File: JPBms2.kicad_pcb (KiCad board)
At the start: 2 copper layers, 65 x 35 mm, 23 parts, among them J1 Conn_ARM_SWD_TagConnect_TC2030, J2 Barrel_Jack_MountingPin, U1 ST715M25R, U2 STM32L053R8Tx, U3 ZXCT1107

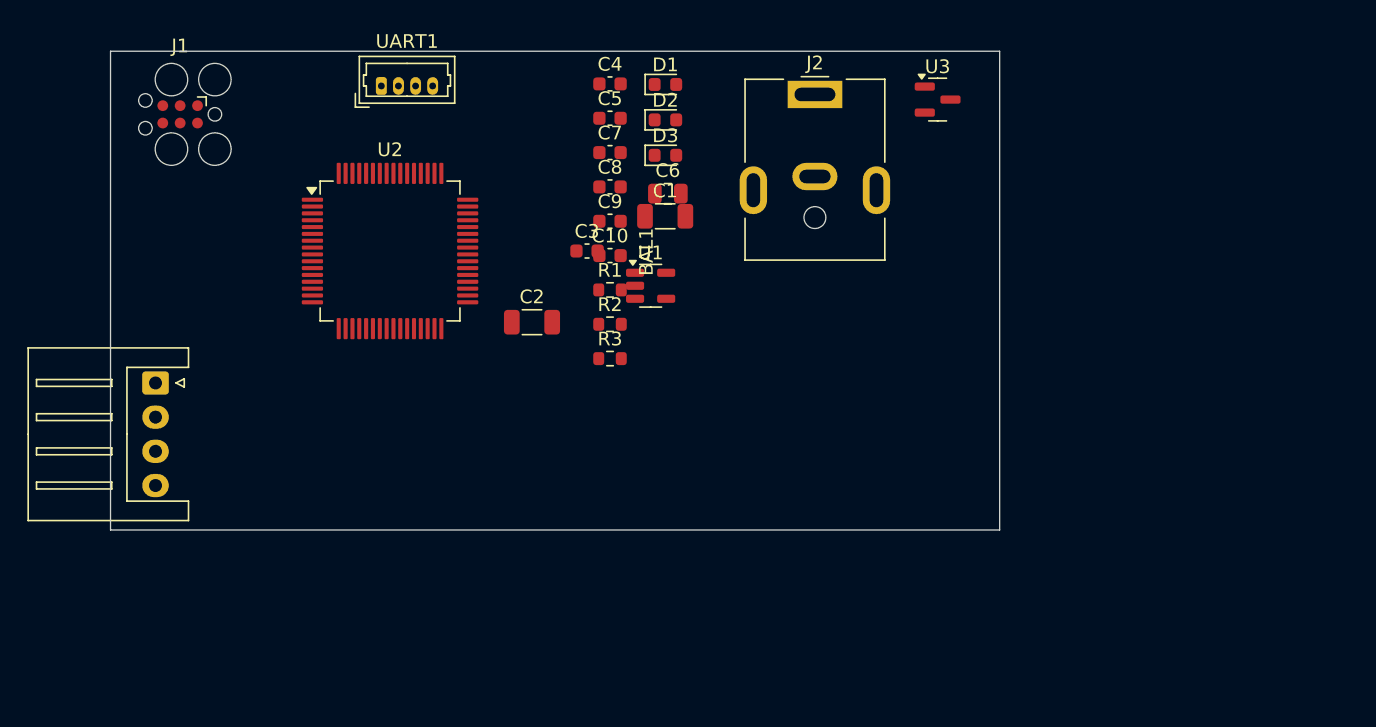
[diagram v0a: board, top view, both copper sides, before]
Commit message: Some part selections
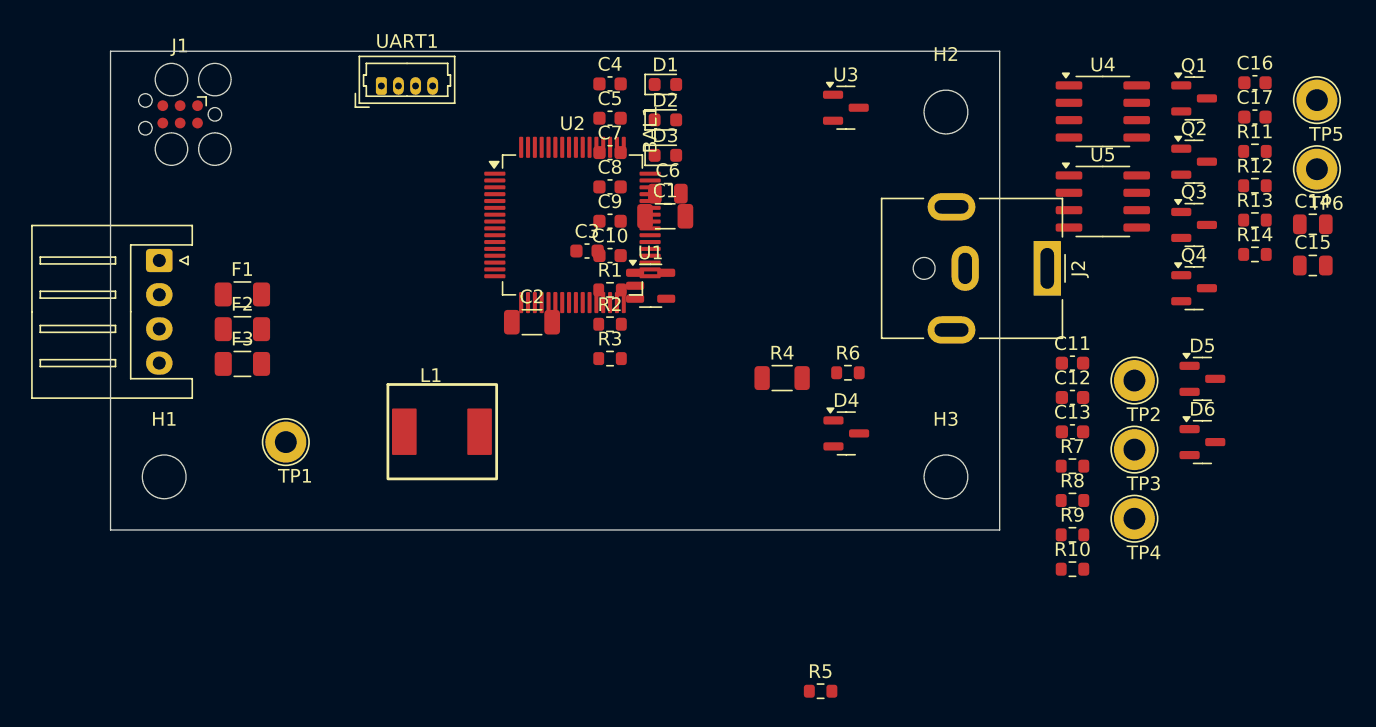
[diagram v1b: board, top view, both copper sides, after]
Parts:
- added C11: 10p, Capacitor_SMD:C_0603_1608Metric, F.Cu at (147.0, 104.1)
- added C12: 1n, Capacitor_SMD:C_0603_1608Metric, F.Cu at (147.0, 106.6)
- added C13: 1n, Capacitor_SMD:C_0603_1608Metric, F.Cu at (147.0, 109.1)
- added C14: 10u, Capacitor_SMD:C_0805_2012Metric, F.Cu at (164.6, 93.9)
- added C15: 10u, Capacitor_SMD:C_0805_2012Metric, F.Cu at (164.6, 96.9)
- added C16: .1u, Capacitor_SMD:C_0603_1608Metric, F.Cu at (160.4, 83.6)
- added C17: .1u, Capacitor_SMD:C_0603_1608Metric, F.Cu at (160.4, 86.1)
- added D4: BAT54S, Package_TO_SOT_SMD:SOT-23, F.Cu at (130.5, 109.2)
- added D5: BAT54S, Package_TO_SOT_SMD:SOT-23, F.Cu at (156.5, 105.2)
- added D6: BAT54S, Package_TO_SOT_SMD:SOT-23, F.Cu at (156.5, 109.9)
- added F1: 30V 750mA, Fuse:Fuse_1206_3216Metric, F.Cu at (86.4, 99.1)
- added F2: 30V 750mA, Fuse:Fuse_1206_3216Metric, F.Cu at (86.4, 101.6)
- added F3: 30V 750mA, Fuse:Fuse_1206_3216Metric, F.Cu at (86.4, 104.1)
- added H1: MountingHole, MountingHole:MountingHole_3.2mm_M3, F.Cu at (80.6, 112.4)
- added H2: MountingHole, MountingHole:MountingHole_3.2mm_M3, F.Cu at (137.8, 85.7)
- added H3: MountingHole, MountingHole:MountingHole_3.2mm_M3, F.Cu at (137.8, 112.4)
- added L1: 220uH, JakeLib:YSPI0630A, F.Cu at (100.9, 109.1)
- added Q1: AO3401A, Package_TO_SOT_SMD:SOT-23, F.Cu at (155.9, 84.7)
- added Q2: AO3401A, Package_TO_SOT_SMD:SOT-23, F.Cu at (155.9, 89.4)
- added Q3: AO3400A, Package_TO_SOT_SMD:SOT-23, F.Cu at (155.9, 94.0)
- added Q4: AO3400A, Package_TO_SOT_SMD:SOT-23, F.Cu at (155.9, 98.6)
- added R10: 39k, Resistor_SMD:R_0603_1608Metric, F.Cu at (147.0, 119.1)
- added R11: 50, Resistor_SMD:R_0603_1608Metric, F.Cu at (160.4, 88.6)
- added R12: 50, Resistor_SMD:R_0603_1608Metric, F.Cu at (160.4, 91.1)
- added R13: 50, Resistor_SMD:R_0603_1608Metric, F.Cu at (160.4, 93.6)
- added R14: 50, Resistor_SMD:R_0603_1608Metric, F.Cu at (160.4, 96.1)
- added R4: 0.25, Resistor_SMD:R_1206_3216Metric, F.Cu at (125.8, 105.2)
- added R5: 4.7k, Resistor_SMD:R_0603_1608Metric, F.Cu at (128.6, 128.1)
- added R6: 1.2k, Resistor_SMD:R_0603_1608Metric, F.Cu at (130.6, 104.8)
- added R7: 200k, Resistor_SMD:R_0603_1608Metric, F.Cu at (147.0, 111.6)
- added R8: 39k, Resistor_SMD:R_0603_1608Metric, F.Cu at (147.0, 114.1)
- added R9: 200k, Resistor_SMD:R_0603_1608Metric, F.Cu at (147.0, 116.6)
- added TP1: TestPoint, TestPoint:TestPoint_Loop_D2.60mm_Drill1.6mm_Beaded, F.Cu at (89.5, 109.9)
- added TP2: TestPoint, TestPoint:TestPoint_Loop_D2.60mm_Drill1.6mm_Beaded, F.Cu at (151.6, 105.4)
- added TP3: TestPoint, TestPoint:TestPoint_Loop_D2.60mm_Drill1.6mm_Beaded, F.Cu at (151.6, 110.4)
- added TP4: TestPoint, TestPoint:TestPoint_Loop_D2.60mm_Drill1.6mm_Beaded, F.Cu at (151.6, 115.5)
- added TP5: TestPoint, TestPoint:TestPoint_Loop_D2.60mm_Drill1.6mm_Beaded, F.Cu at (164.9, 84.9)
- added TP6: TestPoint, TestPoint:TestPoint_Loop_D2.60mm_Drill1.6mm_Beaded, F.Cu at (164.9, 89.9)
- added U4: IRS2003, Package_SO:SOIC-8_3.9x4.9mm_P1.27mm, F.Cu at (149.3, 85.7)
- added U5: IRS2003, Package_SO:SOIC-8_3.9x4.9mm_P1.27mm, F.Cu at (149.3, 92.3)
- moved J2 21.2 mm to (145.2, 97.2), turned to -90 degrees
- moved U2 13.5 mm to (110.5, 94.0)
- moved BAL1 8.95 mm to (80.3, 96.6)
- moved U3 6.73 mm to (130.5, 85.4)
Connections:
- BAL1 pad 2: CELL_4V -> Net-(BAL1-Pin_2)
- BAL1 pad 3: CELL_8V -> Net-(BAL1-Pin_3)
- BAL1 pad 4: CELL_12V -> Net-(BAL1-Pin_4)
- J2 pad 1: Net-(J2-Pad1) -> Net-(U3-Vs+)
- U2 pad 14: unconnected-(U2-PA0-Pad14) -> VSOLAR_ADC
- U2 pad 15: unconnected-(U2-PA1-Pad15) -> VBATT_ADC
- U2 pad 29: unconnected-(U2-PB10-Pad29) -> DD_TOP_B
- U2 pad 30: unconnected-(U2-PB11-Pad30) -> DD_BOT_B
- U2 pad 50: unconnected-(U2-PA15-Pad50) -> DD_TOP_A
- U2 pad 55: unconnected-(U2-PB3-Pad55) -> DD_BOT_A
- U3 pad 1: VSOLAR -> Net-(U3-Vs+)
- U3 pad 3: unconnected-(U3-OUT-Pad3) -> SOLAR_CURRENT_ADC
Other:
- copper layers 2 -> 4
- board text added: "${REFERENCE}"

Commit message: Starting to do layout
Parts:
- J2: footprint Connector_BarrelJack:BarrelJack_CUI_PJ-063AH_Horizontal -> Connector_BarrelJack:BarrelJack_Horizontal
- moved R7 92.7 mm to (54.3, 112.0)
- moved R8 88.9 mm to (58.1, 113.9)
- moved H1 88.8 mm to (156.8, 66.7)
- moved D5 87.1 mm to (69.6, 109.5)
- moved C12 83.5 mm to (63.8, 113.9)
- moved C14 74.1 mm to (116.8, 37.3)
- moved C15 69.8 mm to (128.3, 37.3)
- moved TP4 64.6 mm to (110.3, 65.7)
- moved TP1 61.2 mm to (148.3, 92.7)
- moved C4 60.4 mm to (56.5, 104.5)
- moved TP2 55.4 mm to (104.8, 75.7)
- moved R9 55.0 mm to (92.3, 111.5)
- moved TP3 51.6 mm to (104.8, 88.7)
- moved R10 51.2 mm to (96.1, 113.4)
- moved C3 51.2 mm to (62.2, 109.5)
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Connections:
- U2 pad 16: unconnected-(U2-PA2-Pad16) -> SOLAR_CURRENT_ADC
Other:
- board text removed: "${REFERENCE}"

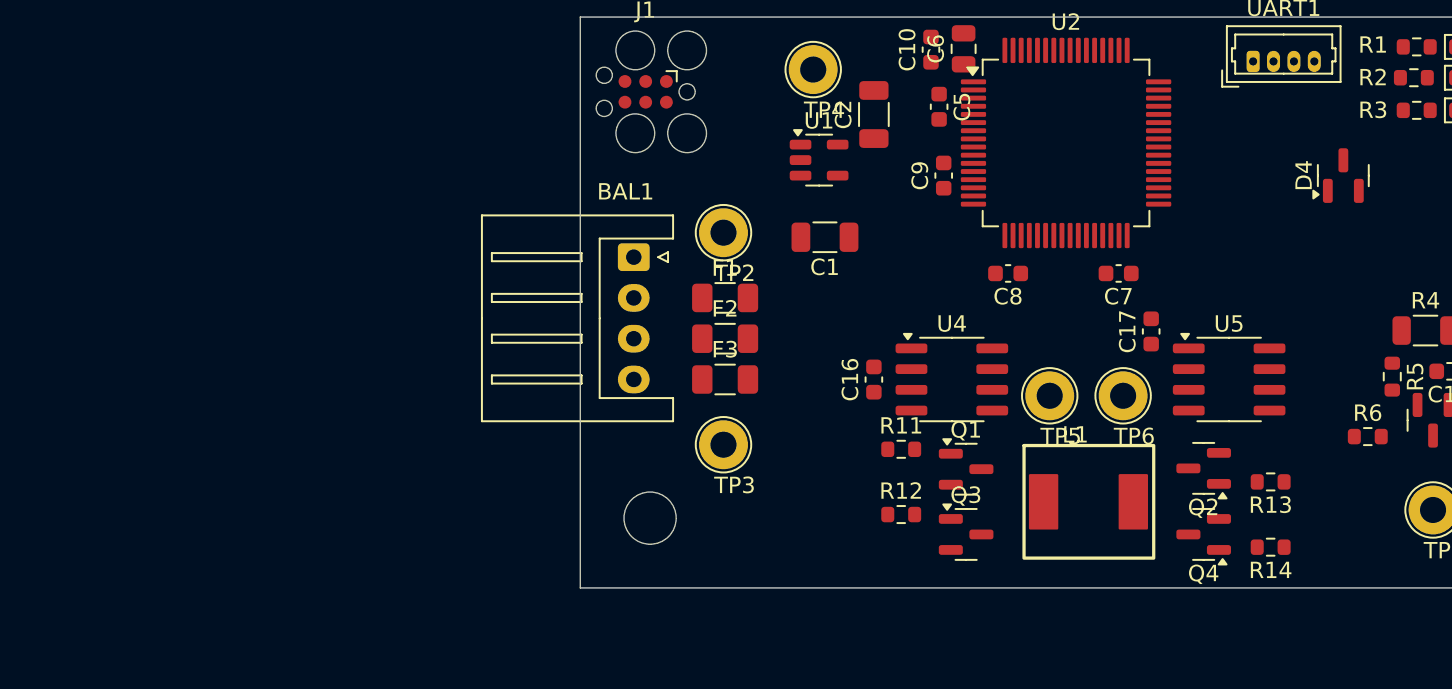
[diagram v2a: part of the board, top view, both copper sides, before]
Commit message: Adding simple balance circuits
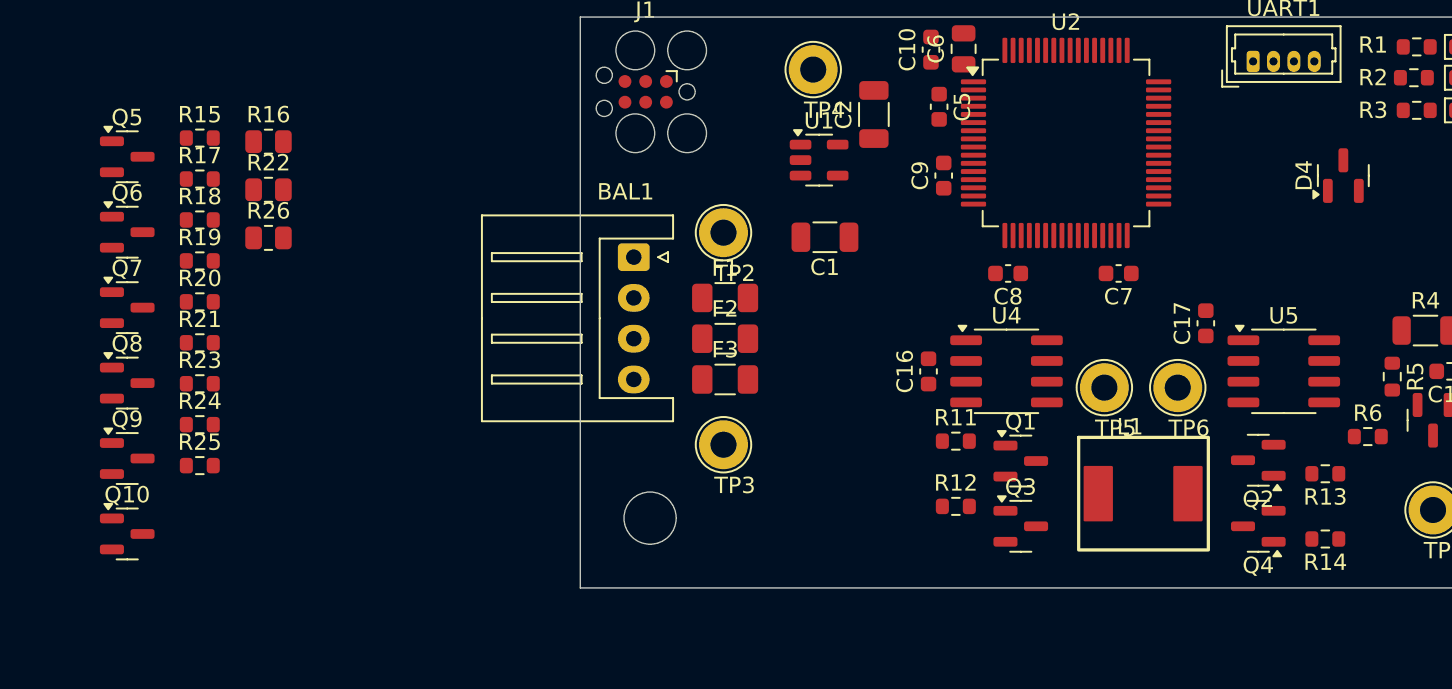
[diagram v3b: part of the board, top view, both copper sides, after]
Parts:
- added Q10: AO3401A, Package_TO_SOT_SMD:SOT-23, F.Cu at (68.2, 94.2)
- added Q5: AO3401A, Package_TO_SOT_SMD:SOT-23, F.Cu at (68.2, 71.1)
- added Q6: AO3400A, Package_TO_SOT_SMD:SOT-23, F.Cu at (68.2, 75.7)
- added Q7: AO3400A, Package_TO_SOT_SMD:SOT-23, F.Cu at (68.2, 80.3)
- added Q8: AO3401A, Package_TO_SOT_SMD:SOT-23, F.Cu at (68.2, 84.9)
- added Q9: AO3400A, Package_TO_SOT_SMD:SOT-23, F.Cu at (68.2, 89.6)
- added R15: 1M, Resistor_SMD:R_0603_1608Metric, F.Cu at (72.7, 69.9)
- added R16: 100, Resistor_SMD:R_0805_2012Metric, F.Cu at (76.9, 70.1)
- added R17: 1M, Resistor_SMD:R_0603_1608Metric, F.Cu at (72.7, 72.4)
- added R18: 1k, Resistor_SMD:R_0603_1608Metric, F.Cu at (72.7, 74.9)
- added R19: 1k, Resistor_SMD:R_0603_1608Metric, F.Cu at (72.7, 77.5)
- added R20: 1M, Resistor_SMD:R_0603_1608Metric, F.Cu at (72.7, 80.0)
- added R21: 1M, Resistor_SMD:R_0603_1608Metric, F.Cu at (72.7, 82.5)
- added R22: 100, Resistor_SMD:R_0805_2012Metric, F.Cu at (76.9, 73.1)
- added R23: 1k, Resistor_SMD:R_0603_1608Metric, F.Cu at (72.7, 85.0)
- added R24: 1M, Resistor_SMD:R_0603_1608Metric, F.Cu at (72.7, 87.5)
- added R25: 1M, Resistor_SMD:R_0603_1608Metric, F.Cu at (72.7, 90.0)
- added R26: 100, Resistor_SMD:R_0805_2012Metric, F.Cu at (76.9, 76.0)
- moved R13 3.39 mm to (141.7, 90.5)
- moved R14 3.39 mm to (141.7, 94.5)
- moved R11 3.39 mm to (119.0, 88.5)
- moved R12 3.39 mm to (119.0, 92.5)
- moved C16 3.39 mm to (117.3, 84.2)
- moved C17 3.39 mm to (134.3, 81.3)
- moved L1 3.39 mm to (130.5, 91.7)
- moved Q1 3.39 mm to (123.0, 89.7)
- moved Q2 3.39 mm to (137.6, 89.7)
- moved Q3 3.39 mm to (123.0, 93.7)
- moved Q4 3.39 mm to (137.6, 93.7)
- moved TP5 3.39 mm to (128.1, 85.2)
- moved TP6 3.39 mm to (132.6, 85.2)
- moved U4 3.39 mm to (122.1, 84.2)
- moved U5 3.39 mm to (139.1, 84.2)
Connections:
- U2 pad 59: unconnected-(U2-PB7-Pad59) -> NBAL_1
- U2 pad 61: unconnected-(U2-PB8-Pad61) -> NBAL_2
- U2 pad 62: unconnected-(U2-PB9-Pad62) -> NBAL_3

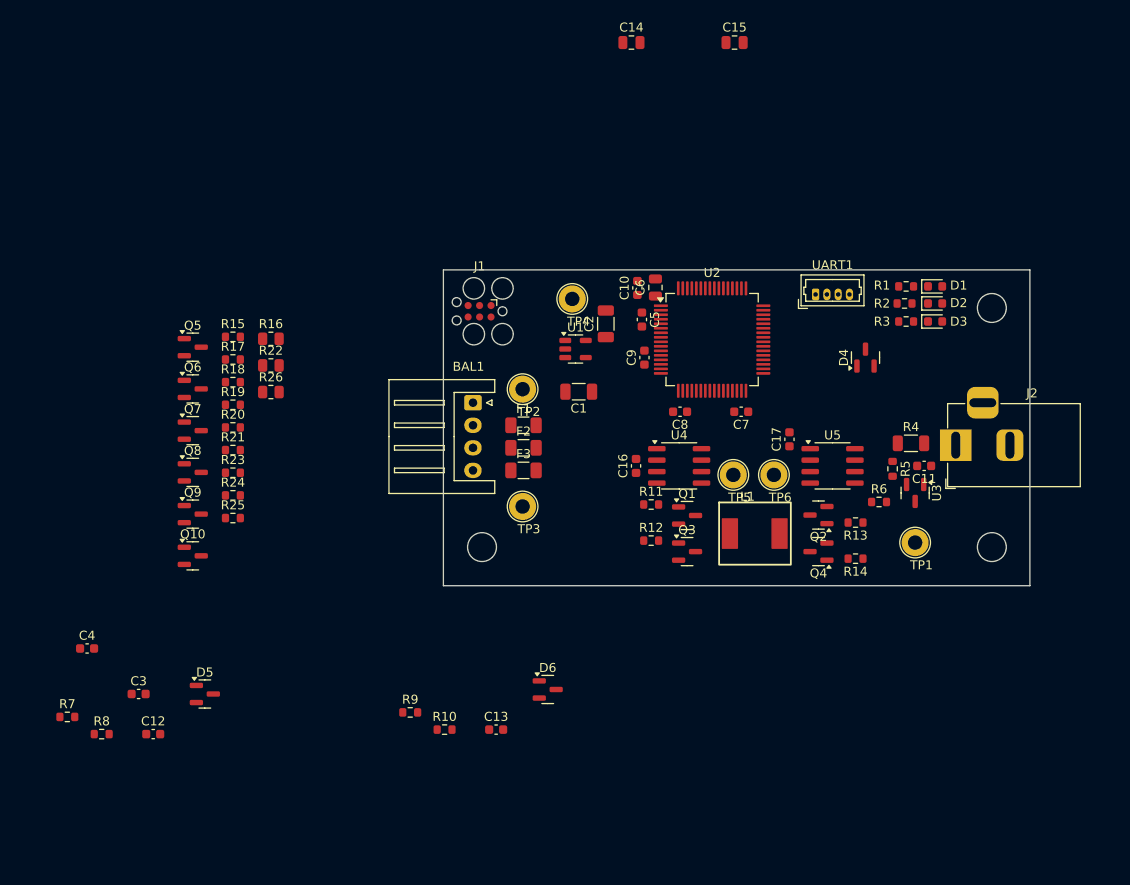
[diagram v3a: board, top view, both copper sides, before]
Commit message: Smaller diodes, more work
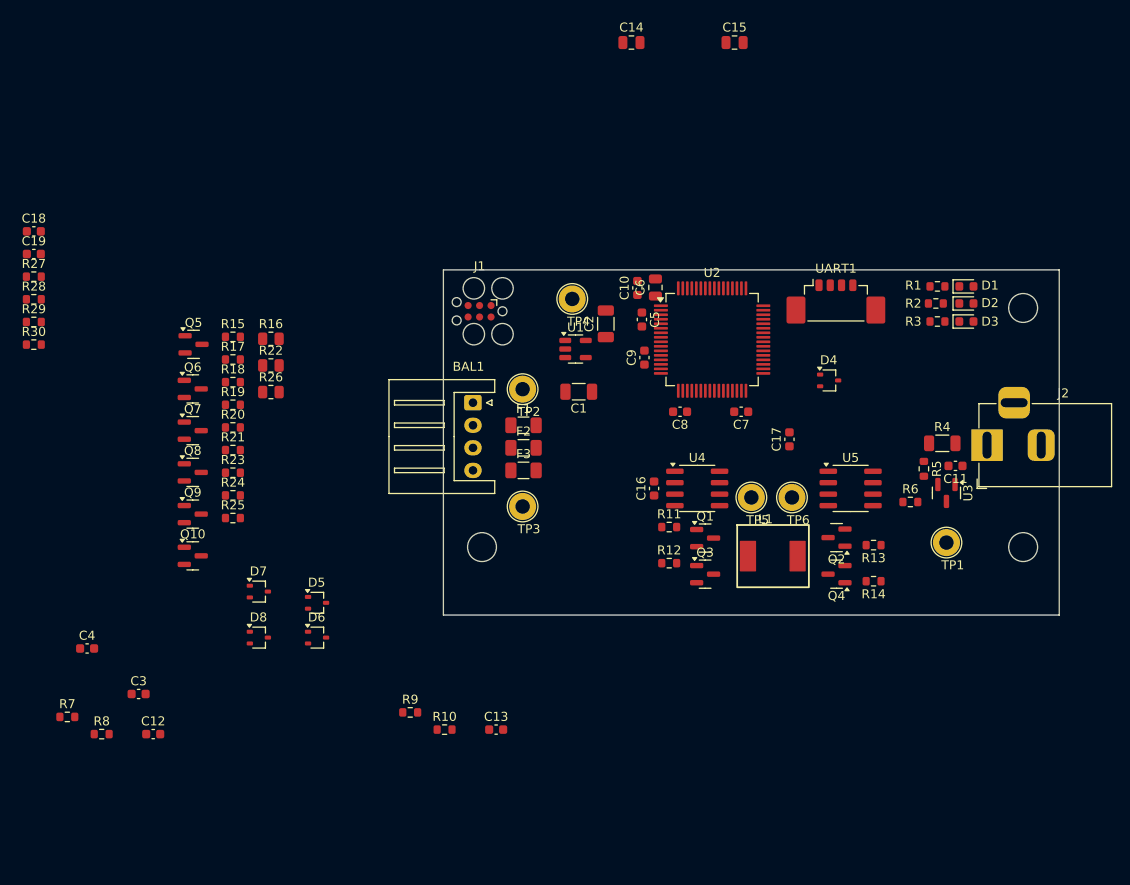
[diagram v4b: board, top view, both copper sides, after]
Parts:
- added C18: 1n, Capacitor_SMD:C_0603_1608Metric, F.Cu at (50.6, 58.2)
- added C19: 1n, Capacitor_SMD:C_0603_1608Metric, F.Cu at (50.6, 60.7)
- added D7: BAT54SW, Package_TO_SOT_SMD:SOT-323_SC-70, F.Cu at (75.5, 98.2)
- added D8: BAT54SW, Package_TO_SOT_SMD:SOT-323_SC-70, F.Cu at (75.5, 103.2)
- added R27: 390k, Resistor_SMD:R_0603_1608Metric, F.Cu at (50.6, 63.2)
- added R28: 150k, Resistor_SMD:R_0603_1608Metric, F.Cu at (50.6, 65.8)
- added R29: 160k, Resistor_SMD:R_0603_1608Metric, F.Cu at (50.6, 68.3)
- added R30: 200k, Resistor_SMD:R_0603_1608Metric, F.Cu at (50.6, 70.8)
- D4, D5, D6: value BAT54S -> BAT54SW; footprint Package_TO_SOT_SMD:SOT-23 -> Package_TO_SOT_SMD:SOT-323_SC-70
- UART1: footprint Connector_Molex:Molex_PicoBlade_53047-0410_1x04_P1.25mm_Vertical -> Connector_Molex:Molex_PicoBlade_53398-0471_1x04-1MP_P1.25mm_Vertical
- moved D6 26.2 mm to (82.0, 103.2)
- moved D5 16.0 mm to (82.0, 99.4)
- moved D4 4.76 mm to (138.8, 74.8), turned to 0 degrees
- moved C11 3.47 mm to (152.8, 84.2)
- moved D1 3.47 mm to (154.0, 64.3)
- moved D2 3.47 mm to (154.0, 66.2)
- moved D3 3.47 mm to (154.0, 68.2)
- moved H1 3.47 mm to (160.2, 66.7)
- moved H3 3.47 mm to (160.2, 93.2)
- moved J2 3.47 mm to (156.2, 81.9)
- moved R1 3.47 mm to (150.8, 64.3)
- moved R2 3.47 mm to (150.6, 66.2)
- moved R3 3.47 mm to (150.8, 68.2)
- moved R4 3.47 mm to (151.3, 81.7)
- moved R5 3.47 mm to (149.2, 84.5)
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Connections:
- net CELL_12V renamed +BATT
- U2 pad 17: unconnected-(U2-PA3-Pad17) -> CELL_4V_ADC
- U2 pad 20: unconnected-(U2-PA4-Pad20) -> CELL_8V_ADC
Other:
- board size 65 x 35 mm -> 68.2 x 38.2 mm

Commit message: Some more placement
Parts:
- removed Q9: AO3400A, Package_TO_SOT_SMD:SOT-23
- added Q11: 2N7002, Package_TO_SOT_SMD:SOT-323_SC-70, F.Cu at (115.1, 91.1)
- Q6, Q7: value AO3400A -> 2N7002; footprint Package_TO_SOT_SMD:SOT-23 -> Package_TO_SOT_SMD:SOT-323_SC-70
- moved Q6 47.8 mm to (115.0, 85.8), turned to 180 degrees
- moved Q5 47.1 mm to (111.2, 90.1), turned to 180 degrees
- moved Q7 46.7 mm to (114.9, 80.3), turned to 180 degrees
- moved R23 45.6 mm to (117.6, 77.4), turned to -90 degrees
- moved R24 45.5 mm to (117.6, 80.5), turned to -90 degrees
- moved Q10 45.2 mm to (110.9, 79.2), turned to 180 degrees
- moved Q8 42.7 mm to (110.9, 84.8), turned to 180 degrees
- moved R22 41.2 mm to (114.9, 88.8)
- moved R25 40.5 mm to (110.9, 76.8)
- moved R16 40.2 mm to (114.8, 83.2)
- moved R26 38.0 mm to (114.9, 77.8)
- moved C1 5.90 mm to (107.5, 71.2), turned to 90 degrees
- moved C17 5.03 mm to (139.0, 83.2), turned to 180 degrees
- moved C16 4.39 mm to (122.0, 83.2), turned to 180 degrees
- moved C2 2.79 mm to (113.8, 71.2)
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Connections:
- Q5 pad 1: Net-(Q5-G) -> Net-(Q11-D)
- Q6 pad 3: Net-(Q5-G) -> Net-(Q6-D)
- Q7 pad 3: Net-(Q7-D) -> Net-(Q10-G)
- Q8 pad 1: Net-(Q7-D) -> Net-(Q6-D)
- R15 pad 2: Net-(Q5-G) -> Net-(Q11-D)
- R17 pad 1: Net-(Q6-G) -> Net-(Q11-G)
- R18 pad 2: Net-(Q6-G) -> Net-(Q11-G)
- R19 pad 2: Net-(Q7-G) -> Net-(Q6-G)
- R20 pad 1: Net-(Q7-G) -> Net-(Q6-G)
- R21 pad 2: Net-(Q7-D) -> Net-(Q6-D)
- R23 pad 2: Net-(Q9-G) -> Net-(Q7-G)
- R24 pad 1: Net-(Q9-G) -> Net-(Q7-G)
